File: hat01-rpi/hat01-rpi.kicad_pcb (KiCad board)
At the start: 2 copper layers, 0 parts

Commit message: hat01-rpi: finish board layout
All components placed and routed.

Could improve:
- Some traces could be rouned around edges
- Some traces should be more parallel (and same length)
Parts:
- added C1: 22p, Capacitor_SMD:C_0402_1005Metric, F.Cu at (89.1, 42.7)
- added C10: 150u, Capacitor_SMD:CP_Elec_6.3x7.7, F.Cu at (80.2, 53.2)
- added C11: 100u, Capacitor_THT:CP_Radial_D8.0mm_P3.50mm, F.Cu at (35.5, 72.2)
- added C2: 22p, Capacitor_SMD:C_0402_1005Metric, F.Cu at (89.1, 40.5)
- added C3: 100n, Capacitor_SMD:C_0402_1005Metric_Pad0.74x0.62mm_HandSolder, F.Cu at (75.4, 36.8)
- added C4: 10n, Capacitor_SMD:C_0402_1005Metric_Pad0.74x0.62mm_HandSolder, F.Cu at (77.2, 48.2)
- added C5: 100n, Capacitor_SMD:C_0402_1005Metric_Pad0.74x0.62mm_HandSolder, F.Cu at (74.0, 46.0)
- added C6: 10u, Capacitor_SMD:C_1206_3216Metric_Pad1.33x1.80mm_HandSolder, F.Cu at (77.0, 67.8)
- added C7: 100u, Capacitor_THT:CP_Radial_D8.0mm_P3.50mm, F.Cu at (85.8, 73.8)
- added C8: 10n, Capacitor_SMD:C_0402_1005Metric_Pad0.74x0.62mm_HandSolder, F.Cu at (80.8, 58.2)
- added C9: 100n, Capacitor_SMD:C_0402_1005Metric_Pad0.74x0.62mm_HandSolder, F.Cu at (83.2, 81.0)
- added D1: GREEN, Exocet:LED_0805_2012Metric_With_Annotations, F.Cu at (36.8, 46.2)
- added D2: YELLOW, Exocet:LED_0805_2012Metric_With_Annotations, F.Cu at (40.1, 46.2)
- added D3: SMBJ5338B, Diode_SMD:D_SMB, F.Cu at (87.2, 51.9)
- added D4: SM4007PL, Diode_SMD:D_SOD-123F, F.Cu at (74.8, 39.8)
- added D5: SS54, Diode_SMD:D_SMA_Handsoldering, F.Cu at (82.5, 63.2)
- added F1: 2A, Exocet:Fuse_Holder_Littelfuse_01530008, F.Cu at (69.2, 73.0)
- added F2: 2A, Fuse:Fuseholder_Clip-5x20mm_Littelfuse_111_Lateral_P18.80x5.00mm_D1.17mm_Horizontal, F.Cu at (59.8, 70.5)
- added H1: 2.75 mm, MountingHole:MountingHole_2.7mm_M2.5, F.Cu at (33.5, 33.5)
- added H2: 2.75 mm, MountingHole:MountingHole_2.7mm_M2.5, F.Cu at (91.5, 33.5)
- added H3: 2.75 mm, MountingHole:MountingHole_2.7mm_M2.5, F.Cu at (33.5, 82.5)
- added H4: 2.75 mm, MountingHole:MountingHole_2.7mm_M2.5, F.Cu at (91.5, 82.5)
- added HS1: Fan, Exocet:RPi_Fan_Mount, F.Cu at (58.0, 53.5)
- added J1: Network Connector, Connector_Molex:Molex_SPOX_5268-05A_1x05_P2.50mm_Horizontal, F.Cu at (59.8, 79.1)
- added J2: RPi_4B_GPIO_Header, Connector_PinSocket_2.54mm:PinSocket_2x20_P2.54mm_Vertical, B.Cu at (38.4, 34.8)
- added J3: USB_A, Connector_USB:USB_A_Molex_67643_Horizontal, F.Cu at (45.2, 72.6)
- added J4: Conn_01x03, Connector_PinHeader_2.54mm:PinHeader_1x03_P2.54mm_Vertical, F.Cu at (40.5, 38.8)
- added JP1: SolderJumper_2_Bridged, Jumper:SolderJumper-2_P1.3mm_Bridged_RoundedPad1.0x1.5mm, B.Cu at (69.7, 38.0)
- added JP2: SolderJumper_2_Bridged, Jumper:SolderJumper-2_P1.3mm_Bridged_RoundedPad1.0x1.5mm, B.Cu at (73.2, 38.0)
- added JP3: SolderJumper_2_Bridged, Jumper:SolderJumper-2_P1.3mm_Bridged_RoundedPad1.0x1.5mm, F.Cu at (39.2, 80.5)
- added L1: 10u, Inductor_SMD:L_Changjiang_FXL0630, F.Cu at (88.8, 66.5)
- added L2: 10u, Inductor_SMD:L_Changjiang_FXL0630, F.Cu at (88.8, 59.2)
- added R1: 8.2k, Resistor_SMD:R_0603_1608Metric_Pad0.98x0.95mm_HandSolder, F.Cu at (75.0, 48.8)
- added R2: 5.6k, Resistor_SMD:R_0603_1608Metric_Pad0.98x0.95mm_HandSolder, F.Cu at (75.5, 45.5)
- added R3: 10k, Resistor_SMD:R_0603_1608Metric_Pad0.98x0.95mm_HandSolder, F.Cu at (74.0, 83.8)
- added R4: 1k, Resistor_SMD:R_0402_1005Metric_Pad0.72x0.64mm_HandSolder, F.Cu at (36.2, 43.8)
- added R5: 1k, Resistor_SMD:R_0402_1005Metric_Pad0.72x0.64mm_HandSolder, F.Cu at (40.7, 42.5)
- added R6: 10k, Resistor_SMD:R_0603_1608Metric_Pad0.98x0.95mm_HandSolder, F.Cu at (75.2, 58.0)
- added R7: 3k, Resistor_SMD:R_0603_1608Metric_Pad0.98x0.95mm_HandSolder, F.Cu at (74.2, 62.2)
- added R8: 220, Resistor_SMD:R_0402_1005Metric, F.Cu at (74.2, 65.0)
- added R9: 1k, Resistor_SMD:R_0402_1005Metric_Pad0.72x0.64mm_HandSolder, F.Cu at (36.2, 42.8)
- added TP1: Loop, TestPoint:TestPoint_Keystone_5005-5009_Compact, F.Cu at (33.0, 45.8)
- added TP10: Loop, TestPoint:TestPoint_Keystone_5005-5009_Compact, F.Cu at (36.9, 55.4)
- added TP11: Loop, TestPoint:TestPoint_Keystone_5005-5009_Compact, F.Cu at (36.9, 63.6)
- added TP12: Loop, TestPoint:TestPoint_Keystone_5005-5009_Compact, F.Cu at (40.2, 67.8)
- added TP13: Pad, TestPoint:TestPoint_Pad_D1.5mm, F.Cu at (66.7, 36.7)
- added TP2: Pad, TestPoint:TestPoint_Pad_D1.5mm, F.Cu at (32.2, 39.5)
- added TP3: Pad, TestPoint:TestPoint_Pad_D1.5mm, F.Cu at (92.0, 38.5)
- added TP4: Pad, TestPoint:TestPoint_Pad_D1.5mm, F.Cu at (82.2, 71.0)
- added TP5: Loop, TestPoint:TestPoint_Keystone_5005-5009_Compact, F.Cu at (92.2, 77.0)
- added TP6: Loop, TestPoint:TestPoint_Keystone_5005-5009_Compact, F.Cu at (86.0, 83.5)
- added TP7: Pad, TestPoint:TestPoint_Pad_D1.5mm, F.Cu at (74.8, 55.5)
- added TP8: Loop, TestPoint:TestPoint_Keystone_5005-5009_Compact, F.Cu at (40.5, 59.8)
- added TP9: Loop, TestPoint:TestPoint_Keystone_5005-5009_Compact, F.Cu at (40.5, 51.6)
- added U1: MCP2515-xSO, Package_SO:SOIC-18W_7.5x11.6mm_P1.27mm, F.Cu at (82.5, 42.0)
- added U2: TPS5430DDA, Package_SO:TI_SO-PowerPAD-8_ThermalVias, F.Cu at (77.9, 62.7)
- added U3: SN65HVD230, Package_SO:SOIC-8_3.9x4.9mm_P1.27mm, F.Cu at (79.0, 81.1)
- added Y1: 8MHz, Exocet:Crystal_SMD_HC49-SD, F.Cu at (92.2, 47.8)
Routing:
- net /MOSI: track 0.00 -> 83.9 mm, vias 0 -> 3
- net /N_CS: track 0.00 -> 79.3 mm, vias 0 -> 4
- net /MISO: track 0.00 -> 77.8 mm, vias 0 -> 4
- net /SCLK: track 0.00 -> 77.3 mm
- net /GPIO25: track 0.00 -> 76.4 mm, vias 0 -> 5
- net /CAN_TX: track 0.00 -> 50.4 mm
- net /CAN_RX: track 0.00 -> 49.0 mm, vias 0 -> 1
- net +3.3V: track 0.00 -> 35.7 mm, vias 0 -> 7
- net Net-(D4-A): track 0.00 -> 20.9 mm, vias 0 -> 3
- net Net-(J3-Shield): track 0.00 -> 19.2 mm
- net Net-(U1-OSC2): track 0.00 -> 15.7 mm
- net /STATUS_LED: track 0.00 -> 13.3 mm
- net +5V: track 0.00 -> 12.4 mm, vias 0 -> 24
- net /CAN_L: track 0.00 -> 12.3 mm, vias 0 -> 1
- net /CAN_H: track 0.00 -> 10.3 mm
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- added copper zone on B.Cu, net +24V
- added copper zone on F.Cu, net +24V
- added copper zone on B.Cu, net +3.3V
- added copper zone on B.Cu, net +5V
- added copper zone on F.Cu, net +5V
- added copper zone on F.Cu, net GND
- added copper zone on F.Cu, net Net-(D5-K)
- added copper zone on B.Cu, net Net-(J1-+24V)
- added copper zone on F.Cu, net Net-(L1-Pad2)
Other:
- board outline added: 65 x 56 mm
- board text added: "${PROJECT_CODE}: ${PROJECT_NAME} (${REVISION})"
- board text added: "F (2A)"

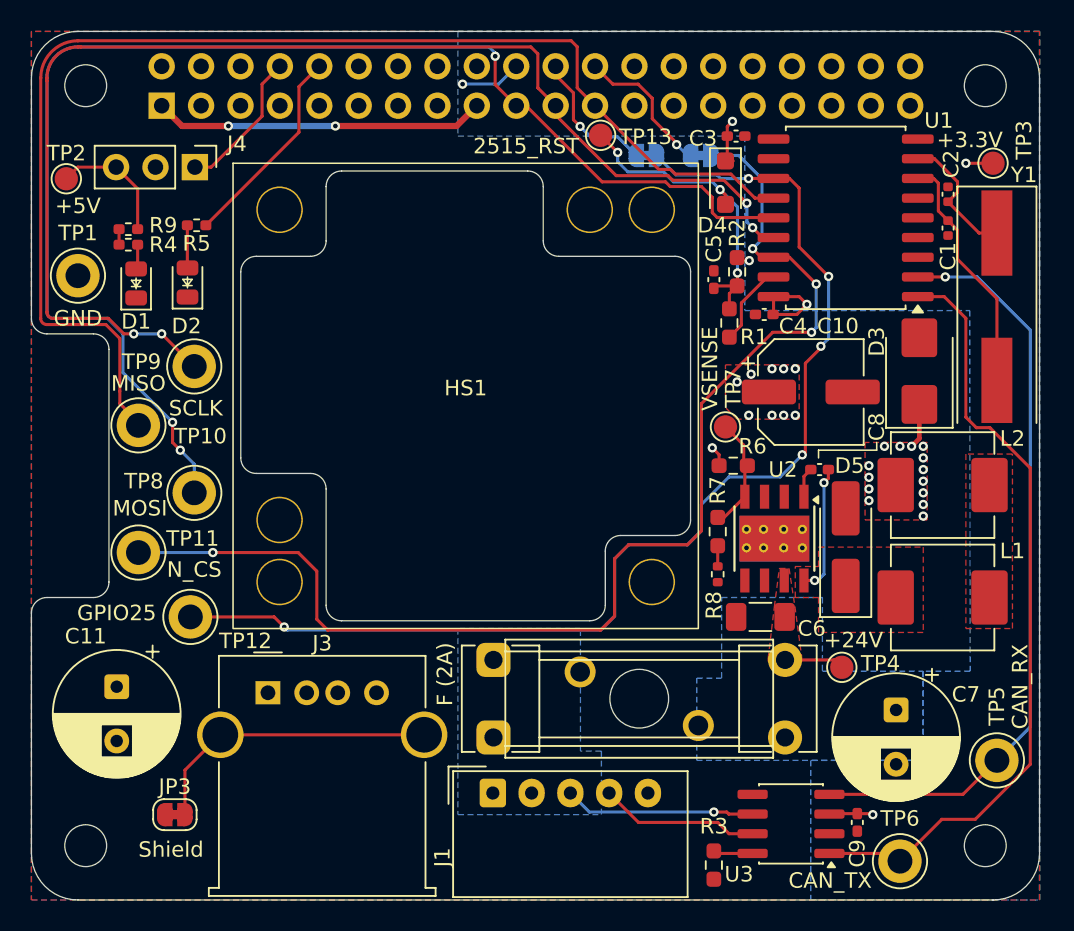
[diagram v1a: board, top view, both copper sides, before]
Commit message: hat01-rpi: minors improvements to board part data
Some components needed to be marked as DNP/exclude from BOM. Finished
rounding some traces around corners. Added some information on the
Silkscreen. This commit was not directly used for the order (this is
v1.1.1, not v1.1.0), but some modifications were added to the previous
version before the order.
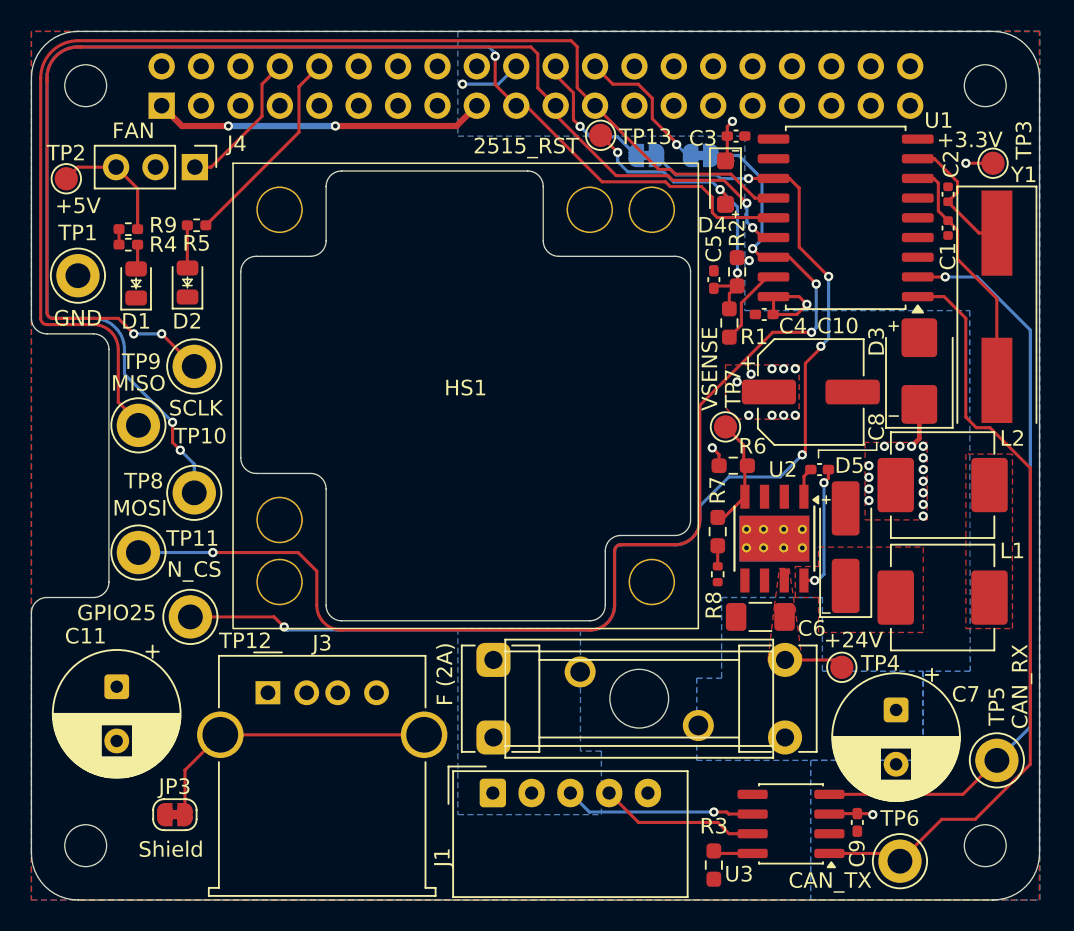
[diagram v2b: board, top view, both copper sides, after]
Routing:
- net /N_CS: track 79.3 -> 70.8 mm
- net /GPIO25: track 76.4 -> 70.7 mm
- net /MOSI: track 83.9 -> 80.6 mm
- net /SCLK: track 77.3 -> 74.5 mm
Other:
- board text added: "FAN"
